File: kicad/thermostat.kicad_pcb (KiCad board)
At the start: 2 copper layers, 108 x 80 mm, 62 parts, among them IC1 LM2596S-5, J1 Display i2c, J6 Screw_Terminal_01x05, T1 SIR424DP, U11 LTC4041, U21 BMP280

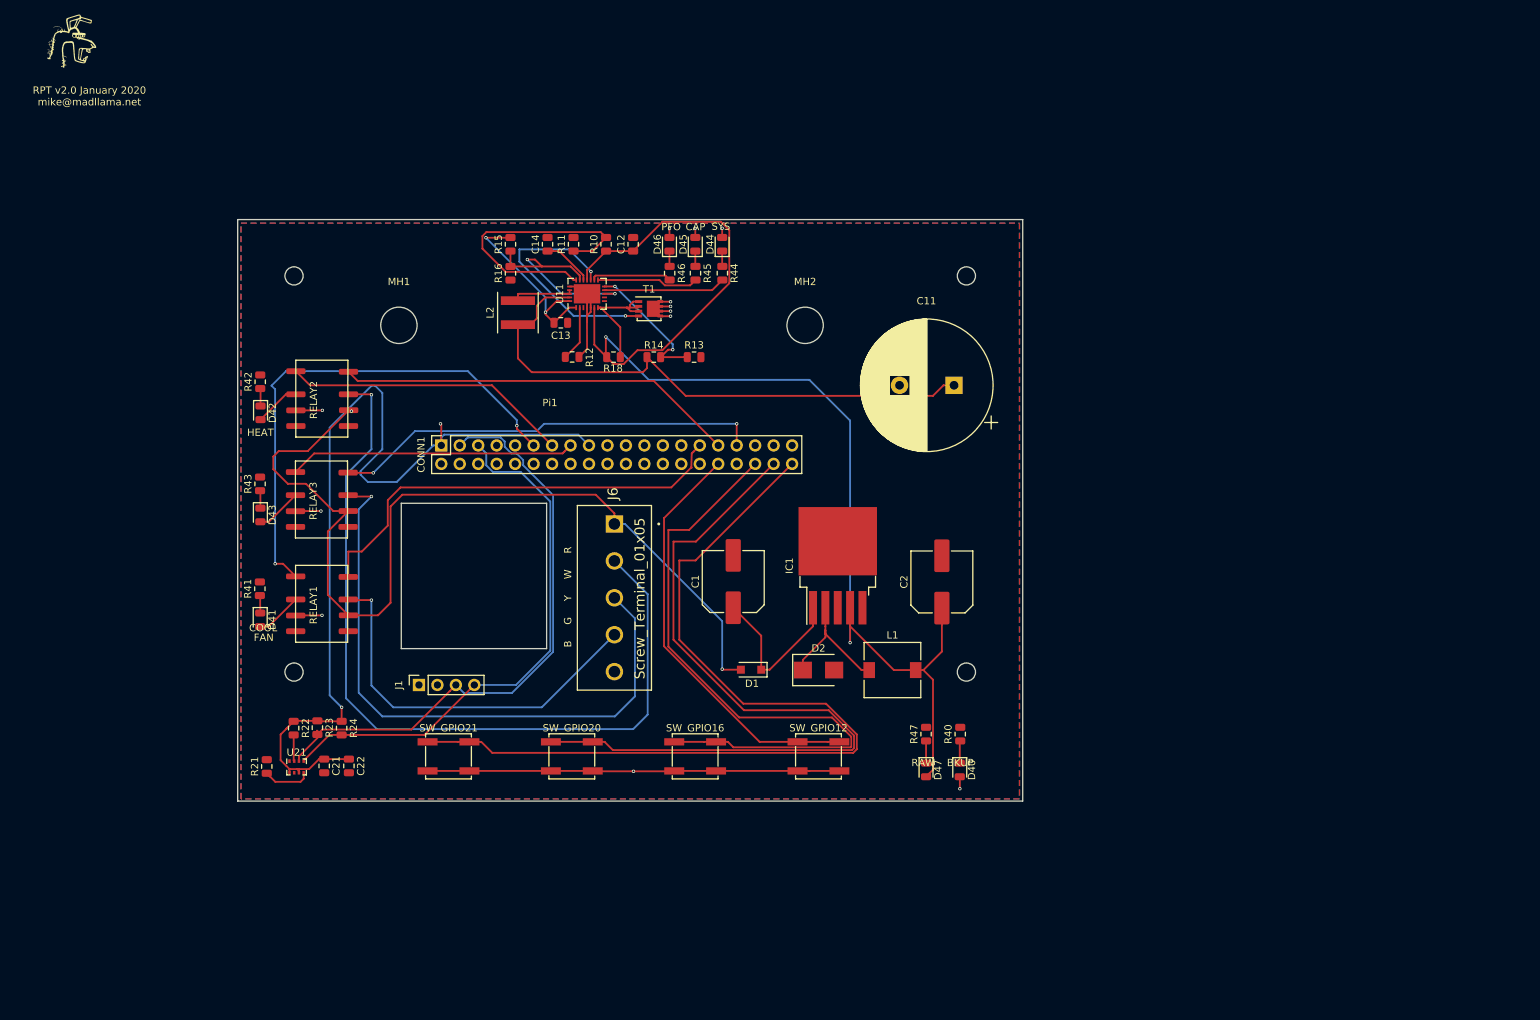
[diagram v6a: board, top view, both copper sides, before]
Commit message: pre-routing of smaller version
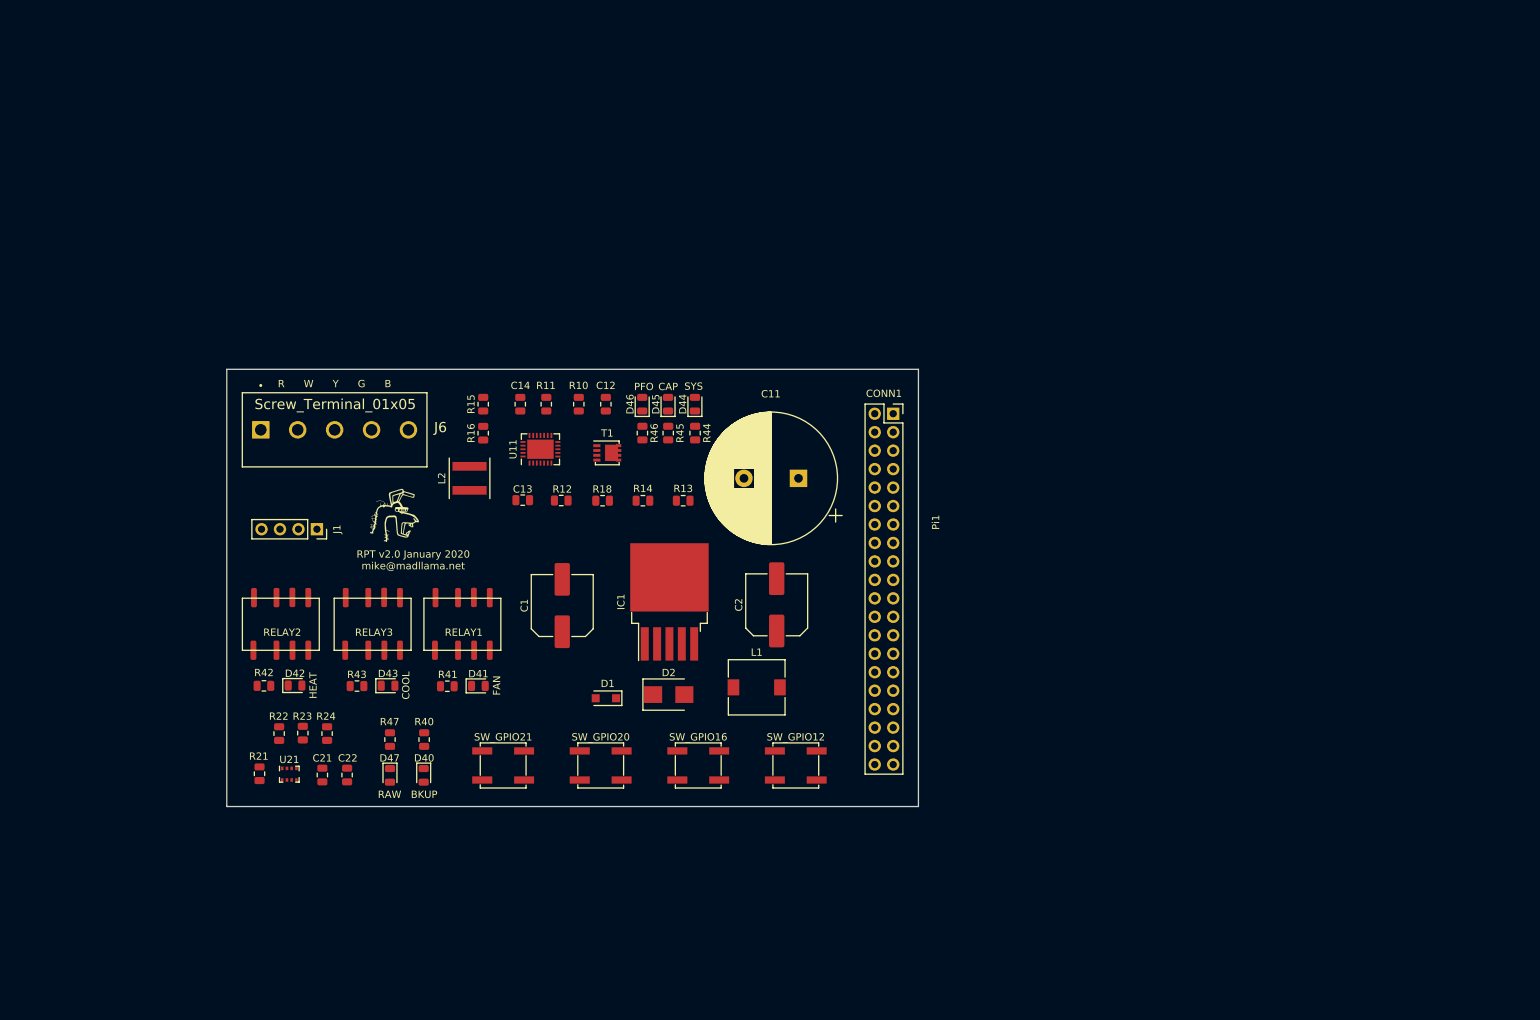
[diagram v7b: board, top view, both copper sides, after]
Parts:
- removed MH1, MH2: Mounting_Hole-Wall, MountingHole:MountingHole_5mm
- removed MK1, MK2, MK3, MK4: Mounting_Hole-Mechanical, MountingHole:MountingHole_2.5mm
- moved Gr1 78.9 mm to (167.5, 151.0)
- moved D40 73.8 mm to (171.4, 186.9)
- moved D47 73.8 mm to (166.8, 186.9)
- moved R40 73.8 mm to (171.5, 181.9)
- moved R47 73.8 mm to (166.8, 181.9)
- moved CONN1 62.3 mm to (236.0, 137.1), turned to 0 degrees
- moved Pi1 56.6 mm to (246.1, 161.1), turned to 270 degrees
- moved J6 50.3 mm to (149.0, 139.3), turned to 0 degrees
- moved R42 41.8 mm to (149.5, 174.6), turned to 180 degrees
- moved D42 37.8 mm to (153.7, 174.5), turned to 0 degrees
- moved RELAY2 31.8 mm to (152.0, 166.7), turned to 0 degrees
- moved D41 31.4 mm to (179.0, 174.6), turned to 0 degrees
- moved R43 30.8 mm to (162.3, 174.6), turned to 180 degrees
- moved D43 29.3 mm to (166.5, 174.5), turned to 0 degrees
- moved R41 29.1 mm to (174.7, 174.6), turned to 180 degrees
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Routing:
- net /PWR_5V_RAW: track 177.7 -> 0.00 mm, vias 2 -> 0
- net /HVAC_PWR(RED): track 127.5 -> 0.00 mm, vias 2 -> 0
- net /PWR_3.3V: track 127.0 -> 0.00 mm, vias 2 -> 0
- net /GPIO21(SPI1_SCK): track 123.7 -> 0.00 mm
- net /HVAC_HEAT(WHITE): track 113.5 -> 0.00 mm, vias 1 -> 0
- net /PWR_5V: track 110.5 -> 0.00 mm, vias 14 -> 0
- net /GPIO20(SPI1_MOSI): track 106.0 -> 0.00 mm
- net /GPIO16: track 88.2 -> 0.00 mm
- net /HVAC_COOL(YELLOW): track 86.2 -> 0.00 mm, vias 1 -> 0
- net /GPIO2(SDA1): track 82.3 -> 0.00 mm
- net Net-(C11-Pad1): track 79.7 -> 0.00 mm
- net /GPIO3(SCL1): track 74.8 -> 0.00 mm
- net /GPIO17(GEN0): track 70.1 -> 0.00 mm, vias 2 -> 0
- net /GPIO5: track 61.1 -> 0.00 mm
- net /GPIO13(PWM1): track 59.2 -> 0.00 mm, vias 2 -> 0
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- removed copper zone on B.Cu, net /PWR_5V
- removed copper zone on F.Cu, net GND
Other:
- board size 108 x 80 mm -> 95.2 x 60.2 mm
- board text added: "R W Y G B"
- board text removed: "B G Y W R"

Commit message: updates, close to thermostat v2.1
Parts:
- moved R44 2.75 mm to (208.8, 142.5)
- moved R45 2.75 mm to (205.1, 142.5)
- moved R46 2.75 mm to (201.5, 142.5)
- moved C11 2.15 mm to (224.8, 144.8)
- moved T1 0.69 mm to (196.0, 142.5)
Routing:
- net /PWR_5V_RAW: track 0.00 -> 194.1 mm, vias 0 -> 3
- net /GPIO3(SCL1): track 0.00 -> 151.3 mm, vias 0 -> 1
- net /PWR_3.3V: track 0.00 -> 149.4 mm, vias 0 -> 1
- net /GPIO2(SDA1): track 0.00 -> 136.2 mm
- net /GPIO27(GEN2): track 0.00 -> 109.0 mm, vias 0 -> 1
- net /GPIO17(GEN0): track 0.00 -> 107.2 mm, vias 0 -> 1
- net /GPIO6: track 0.00 -> 101.4 mm, vias 0 -> 1
- net /GPIO22(GEN3): track 0.00 -> 93.1 mm, vias 0 -> 1
- net /GPIO13(PWM1): track 0.00 -> 84.7 mm, vias 0 -> 1
- net /HVAC_PWR(RED): track 0.00 -> 81.7 mm, vias 0 -> 2
- net /PWR_5V: track 0.00 -> 80.2 mm, vias 0 -> 16
- net /GPIO5: track 0.00 -> 71.3 mm, vias 0 -> 1
- net Net-(C11-Pad1): track 0.00 -> 63.8 mm
- net /GPIO21(SPI1_SCK): track 0.00 -> 55.9 mm
- net Net-(R15-Pad1): track 0.00 -> 45.5 mm, vias 0 -> 2
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- added copper zone on B.Cu, net /PWR_5V
- added copper zone on F.Cu, net GND
